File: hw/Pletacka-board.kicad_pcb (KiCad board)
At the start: 2 copper layers, 15 parts, among them SW1 SW_Push_Dual_x2, SW2 SW_Push_Dual_x2, SW3 SW_Push_Dual_x2, U1 EL357N(A)(TA)-G, U2 EL357N(A)(TA)-G

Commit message: Add connectors
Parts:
- added D3: B5819W, B5819W:B5819W_SOD-123, F.Cu at (110.6, 71.2)
- added D4: SS34, SS34:DIOM7959X265N, F.Cu at (93.8, 68.0)
- added D5: 1SMB5935BT3G, 1SMB5935BT3G:DIOM5436X247N, F.Cu at (92.6, 74.3)
- added J3: Conn_01x01_Female, TerminalBlock:TerminalBlock_Altech_AK300-2_P5.00mm, F.Cu at (79.1, 71.3)
- added J4: Conn_01x02_Female, Terminal_block:TerminalBlock_Phoenix_PT-1,5-2-5.0-H_1x02_P5.00mm_Horizontal, F.Cu at (121.7, -20.9)
- added J5: Conn_01x03_Female, Terminal_block:TerminalBlock_Phoenix_PT-1,5-3-5.0-H_1x03_P5.00mm_Horizontal, F.Cu at (104.6, -20.9)
- added POLYFUSE1: 24V 1A, Resistor_SMD:R_1206_3216Metric, F.Cu at (90.7, 78.5)
- added REF**: TerminalBlock_Phoenix_PT-1,5-2-5.0-H_1x02_P5.00mm_Horizontal, Terminal_block:TerminalBlock_Phoenix_PT-1,5-2-5.0-H_1x02_P5.00mm_Horizontal, F.Cu at (180.3, 30.5)
- added U1: EL357N(A)(TA)-G, EL357N_A__TA_-G:SOP254P700X200-4N, F.Cu at (113.2, 67.1)
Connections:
- net Net-(U2-Pad4) renamed /Optocoupler/OPTO_FINSIH
- C1 pad 2: GND -> OPTO_FINISHED_IN_MINUS
- C2 pad 2: GND -> OPTO_FINISHED_IN_MINUS
- C3 pad 2: GND -> OPTO_FINISHED_IN_MINUS
- D1 pad 1: GND -> OPTO_FINISHED_IN_MINUS
- E1 pad G1: GND -> OPTO_FINISHED_IN_MINUS
- E1 pad G2: GND -> OPTO_FINISHED_IN_MINUS
- E1 pad G3: GND -> OPTO_FINISHED_IN_MINUS
- E1 pad G4: GND -> OPTO_FINISHED_IN_MINUS
- E1 pad G5: GND -> OPTO_FINISHED_IN_MINUS
- SW1 pad 2: GND -> OPTO_FINISHED_IN_MINUS
- SW2 pad 2: GND -> OPTO_FINISHED_IN_MINUS
- SW3 pad 2: GND -> OPTO_FINISHED_IN_MINUS
- U2 pad 1: Net-(U2-Pad1) -> Net-(D2-PadC)
- U2 pad 2: Net-(U2-Pad2) -> Net-(D2-PadA)
- U2 pad 3: Net-(U2-Pad3) -> OPTO_FINISHED_IN_MINUS

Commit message: Update some packages, add 3D models
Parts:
- removed J3: Conn_01x01_Female, TerminalBlock:TerminalBlock_Altech_AK300-2_P5.00mm
- removed REF**: TerminalBlock_Phoenix_PT-1,5-2-5.0-H_1x02_P5.00mm_Horizontal, Terminal_block:TerminalBlock_Phoenix_PT-1,5-2-5.0-H_1x02_P5.00mm_Horizontal
- removed the U1 at (113.2, 67.1)
- removed the U1 at (166.4, 127.0)
- added C4: 10u/50V, Capacitor_SMD:C_0603_1608Metric, F.Cu at (132.3, 80.8)
- added C5: 33n, Capacitor_SMD:C_0603_1608Metric, F.Cu at (132.3, 83.3)
- added C6: 22n, Capacitor_SMD:C_0603_1608Metric, F.Cu at (136.3, 80.8)
- added C7: 8.2n, Capacitor_SMD:C_0603_1608Metric, F.Cu at (132.3, 85.8)
- added C8: 100n, Capacitor_SMD:C_0603_1608Metric, F.Cu at (136.3, 83.3)
- added C9: 22u, Capacitor_SMD:C_0603_1608Metric, F.Cu at (140.3, 80.8)
- added D6: LED, LED_SMD:LED_0603_1608Metric, F.Cu at (122.6, 81.3)
- added D7: SS34, SS34:DIOM7959X265N, F.Cu at (159.1, 94.0)
- added H1: MountingHole, MountingHole:MountingHole_2.7mm_M2.5_Pad, F.Cu at (119.4, 135.9)
- added H2: MountingHole, MountingHole:MountingHole_2.7mm_M2.5_Pad, F.Cu at (143.5, 66.0)
- added R10: 100-OH, Resistor_SMD:R_0603_1608Metric, F.Cu at (136.3, 85.8)
- added R11: R, Resistor_SMD:R_0603_1608Metric, F.Cu at (140.3, 83.3)
- added R12: R, Resistor_SMD:R_0603_1608Metric, F.Cu at (140.3, 85.8)
- added R5: 20k, Resistor_SMD:R_0603_1608Metric, F.Cu at (125.7, 104.1)
- added R6: 20k, Resistor_SMD:R_0603_1608Metric, F.Cu at (129.7, 104.1)
- added R7: 10k, Resistor_SMD:R_0603_1608Metric, F.Cu at (134.6, 95.9)
- added R8: 10k, Resistor_SMD:R_0603_1608Metric, F.Cu at (140.8, 90.6)
- added R9: 2k2, Resistor_SMD:R_0603_1608Metric, F.Cu at (126.6, 83.8)
- added U1: EL357N(A)(TA)-G, EL357N_A__TA_-G:SOP254P700X200-4N, F.Cu at (132.2, 86.1)
- added U3: TPS54231D, TPS54231D:SOIC127P599X175-8N, F.Cu at (125.3, 73.7)
- SW1, SW2: footprint Button_Switch_SMD:SW_SPST_SKQG_WithStem -> Button_SMD:SW_SPST_SKQG_WithStem
- SW3: footprint Resistor_SMD:R_0603_1608Metric -> Button_SMD:SW_SPST_SKQG_WithStem
- moved J5 166.9 mm to (133.3, 143.5)
- moved J4 164.4 mm to (123.2, 143.5)
- moved U2 124.4 mm to (137.2, 109.2)
- moved D2 79.4 mm to (116.9, 64.3)
- moved C1 77.9 mm to (126.8, 119.0)
- moved SW3 75.0 mm to (117.5, 111.2), turned to 90 degrees
- moved D4 74.6 mm to (159.1, 104.1)
- moved D5 62.3 mm to (154.9, 76.2)
- moved SW2 58.2 mm to (117.5, 101.0), turned to 90 degrees
- moved POLYFUSE1 50.7 mm to (141.1, 72.1)
- moved E1 34.2 mm to (133.3, 96.5), turned to 180 degrees
- moved R3 34.1 mm to (122.8, 119.0)
- moved SW1 32.2 mm to (117.4, 90.9), turned to 90 degrees
- moved R1 30.3 mm to (122.8, 121.5)
- moved C2 26.8 mm to (122.8, 124.0)
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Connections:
- net Net-(E1-Pad36) renamed OPTO_FINSIHED
- D2 pad A: Net-(D2-PadA) -> OPTO_FINISHED_IN_MINUS
- D3 pad A: Net-(D3-PadA) -> OPTO_STOP_IN_MINUS
- D4 pad A: Net-(D4-PadA) -> VCC
- D5 pad A: Net-(D5-PadA) -> OPTO_FINISHED_IN_MINUS
- E1 pad 12: Net-(E1-Pad12) -> BTN_2
- E1 pad 13: Net-(E1-Pad13) -> BTN_RESET
- E1 pad 21: Net-(E1-Pad21) -> BTN_1
- E1 pad 37: Net-(E1-Pad37) -> OPTO_STOP
- U2 pad 1: Net-(D2-PadC) -> Net-(D3-PadC)
- U2 pad 2: Net-(D2-PadA) -> OPTO_STOP_IN_MINUS
- U2 pad 4: /Optocoupler/OPTO_FINSIH -> OPTO_STOP

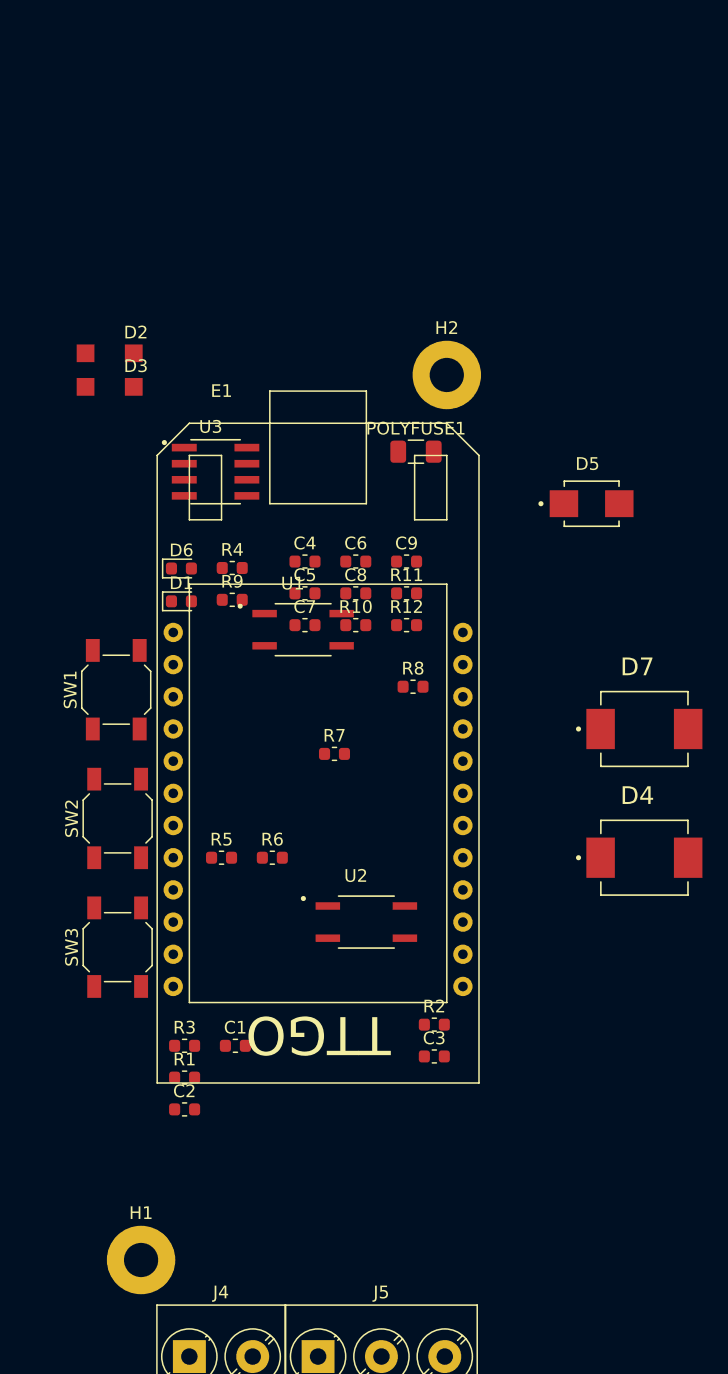
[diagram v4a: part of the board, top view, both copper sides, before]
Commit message: Update some packages
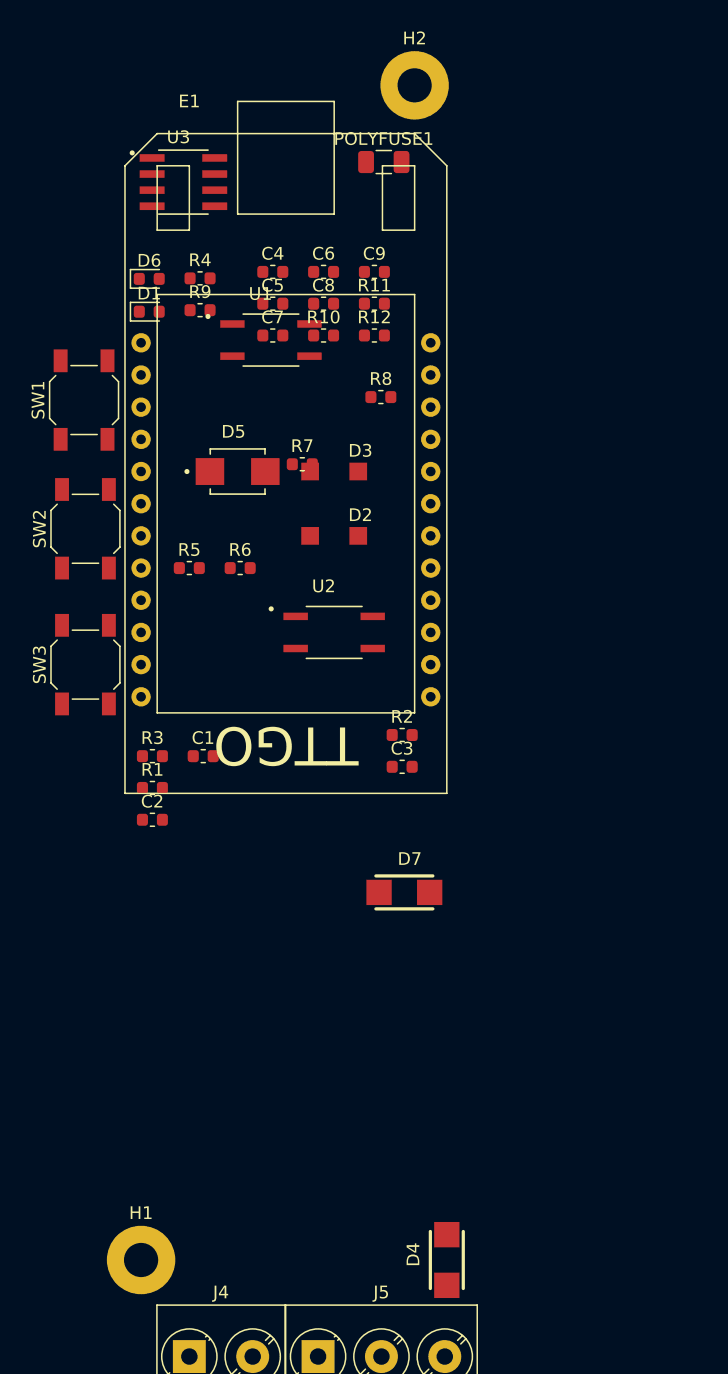
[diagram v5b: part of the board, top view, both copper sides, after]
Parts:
- D4, D7: footprint SS34:DIOM7959X265N -> SS34:SMA
- moved D4 35.4 mm to (143.5, 135.9), turned to 90 degrees
- moved D5 28.1 mm to (127.0, 73.7)
- moved C5 23.0 mm to (129.8, 60.4)
- moved C8 23.0 mm to (133.8, 60.4)
- moved H2 23.0 mm to (141.0, 43.2)
- moved R11 23.0 mm to (137.8, 60.4)
- moved R4 23.0 mm to (124.0, 58.4)
- moved R7 23.0 mm to (132.1, 73.1)
- moved U3 23.0 mm to (122.7, 50.8)
- moved C1 23.0 mm to (124.3, 96.1)
- moved C2 23.0 mm to (120.3, 101.1)
- moved C3 23.0 mm to (140.0, 97.0)
- moved C4 23.0 mm to (129.8, 57.9)
- moved C6 23.0 mm to (133.8, 57.9)
- moved C9 23.0 mm to (137.8, 57.9)
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
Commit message: Routing schema
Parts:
- removed C3: 100n, Capacitor_SMD:C_0603_1608Metric
- removed R3: 2k2, Resistor_SMD:R_0603_1608Metric
- removed SW2: SW_Push_Dual_x2, Button_SMD:SW_SPST_SKQG_WithStem
- added L1: L, Inductor_SMD:L_TDK_SLF7045, F.Cu at (141.0, 123.8)
- C4: footprint Capacitor_SMD:C_0603_1608Metric -> Capacitor_SMD:C_1206_3216Metric
- moved POLYFUSE1 87.9 mm to (138.4, 137.2), turned to 180 degrees
- moved U3 81.9 mm to (137.2, 131.4)
- moved D3 79.4 mm to (91.4, 140.3)
- moved R8 78.2 mm to (89.5, 128.9)
- moved U1 76.4 mm to (102.2, 134.6), turned to 90 degrees
- moved C6 74.4 mm to (144.1, 131.6), turned to 90 degrees
- moved R9 73.5 mm to (64.1, 103.5), turned to 180 degrees
- moved R4 73.1 mm to (64.1, 100.3), turned to 180 degrees
- moved R6 72.7 mm to (89.5, 143.5), turned to 270 degrees
- moved C5 72.3 mm to (142.2, 131.6), turned to 90 degrees
- moved C4 71.7 mm to (132.1, 129.5), turned to 90 degrees
- moved R10 71.7 mm to (143.0, 134.0)
- moved C7 70.6 mm to (132.6, 133.5), turned to 90 degrees
- moved D2 69.9 mm to (101.6, 140.3)
- moved D6 69.3 mm to (67.3, 103.5), turned to 180 degrees
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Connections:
- net OPTO_FINISHED_IN_MINUS renamed GND
- E1 pad 12: BTN_2 -> Net-(E1-Pad12)
- R7 pad 2: /Optocoupler/OPTO_FINSIH_OUT -> OPTO_FINSIHED
- U1 pad 4: /Optocoupler/OPTO_FINSIH_OUT -> OPTO_FINSIHED
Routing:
- net Net-(R11-Pad2): track 0.00 -> 13.9 mm
- net +24V: track 0.00 -> 13.4 mm
- net Net-(C8-Pad2): track 0.00 -> 10.5 mm
- net +3V3: track 0.00 -> 8.93 mm
- net VCC: track 0.00 -> 7.51 mm
- net GND: track 0.00 -> 6.42 mm
- net Net-(C1-Pad1): track 0.00 -> 6.16 mm
- net Net-(C2-Pad1): track 0.00 -> 5.52 mm
- net Net-(C5-Pad1): track 0.00 -> 4.34 mm
- net Net-(C7-Pad1): track 0.00 -> 2.48 mm
- net Net-(D4-PadC): track 0.00 -> 2.31 mm
- net Net-(C6-Pad1): track 0.00 -> 1.74 mm
- net Net-(C8-Pad1): track 0.00 -> 1.12 mm
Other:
- board outline added: 29 x 80.2 mm

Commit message: Routing board
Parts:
- moved R4 57.3 mm to (120.7, 90.8), turned to 90 degrees
- moved R9 56.5 mm to (120.7, 102.2), turned to 270 degrees
- moved D1 53.6 mm to (120.7, 94.6), turned to 90 degrees
- moved D6 53.6 mm to (120.7, 98.4), turned to 270 degrees
- moved H1 36.3 mm to (134.6, 104.1)
- moved R8 33.3 mm to (122.6, 124.9), turned to 270 degrees
- moved D3 32.5 mm to (123.8, 137.2)
- moved U1 32.4 mm to (130.8, 119.4)
- moved U2 31.9 mm to (123.8, 131.4)
- moved D2 31.8 mm to (129.5, 125.1)
- moved R5 31.7 mm to (127.6, 128.1)
- moved R6 31.2 mm to (120.0, 137.0)
- moved R7 27.7 mm to (126.4, 119.4), turned to 180 degrees
- moved D7 3.10 mm to (137.7, 127.0), turned to 180 degrees
- moved L1 2.54 mm to (141.0, 121.3)
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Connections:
- E1 pad 25: Net-(E1-Pad25) -> LED_SEND
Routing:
- net OPTO_FINISHED_IN_PLUS: track 0.00 -> 25.9 mm
- net +3V3: track 8.93 -> 33.6 mm
- net OPTO_STOP: track 0.00 -> 15.5 mm
- net Net-(C8-Pad1): track 1.12 -> 14.7 mm, vias 0 -> 2
- net Net-(C8-Pad2): track 10.5 -> 0.00 mm
- net OPTO_STOP_IN_MINUS: track 0.00 -> 10.3 mm
- net OPTO_FINSIHED: track 0.00 -> 7.89 mm
- net OPTO_STOP_IN_PLUS: track 0.00 -> 7.24 mm
- net Net-(D2-PadC): track 0.00 -> 6.36 mm
- net Net-(D3-PadC): track 0.00 -> 5.24 mm
- net GND: track 6.42 -> 11.1 mm, vias 0 -> 5
- net LED_SEND: track 0.00 -> 3.26 mm
- net Net-(D6-Pad2): track 0.00 -> 2.23 mm
- net Net-(D1-Pad2): track 0.00 -> 2.23 mm
- added copper zone on F.Cu, net Net-(C8-Pad2)
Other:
- rule via_min_size: 0.4 -> 0.45
- board text added: "Ledky presunout nahoru Pridat krydelka Zmenit tlacitka Zkontrolovat LCSC"
